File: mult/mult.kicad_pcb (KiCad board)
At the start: 2 copper layers, 20 x 108 mm, 72 parts, among them J1 Eurorack_Mono_Jack, J10 Eurorack_Mono_Jack, J11 Eurorack_Mono_Jack_No_S, J12 Eurorack_Mono_Jack_No_S, J13 Eurorack_Mono_Jack, J14 Eurorack_Mono_Jack, J15 Eurorack_Mono_Jack_No_S, J16 Eurorack_Mono_Jack_No_S, J17 Eurorack_Power, J2 Eurorack_Mono_Jack, J3 Eurorack_Mono_Jack_No_S, J4 Eurorack_Mono_Jack_No_S, J6 Eurorack_Mono_Jack, J7 Eurorack_Mono_Jack_No_S, J8 Eurorack_Mono_Jack_No_S, J9 Eurorack_Mono_Jack, U1 OPA1679, U2 OPA1679, U3 OPA1679, U4 OPA1679

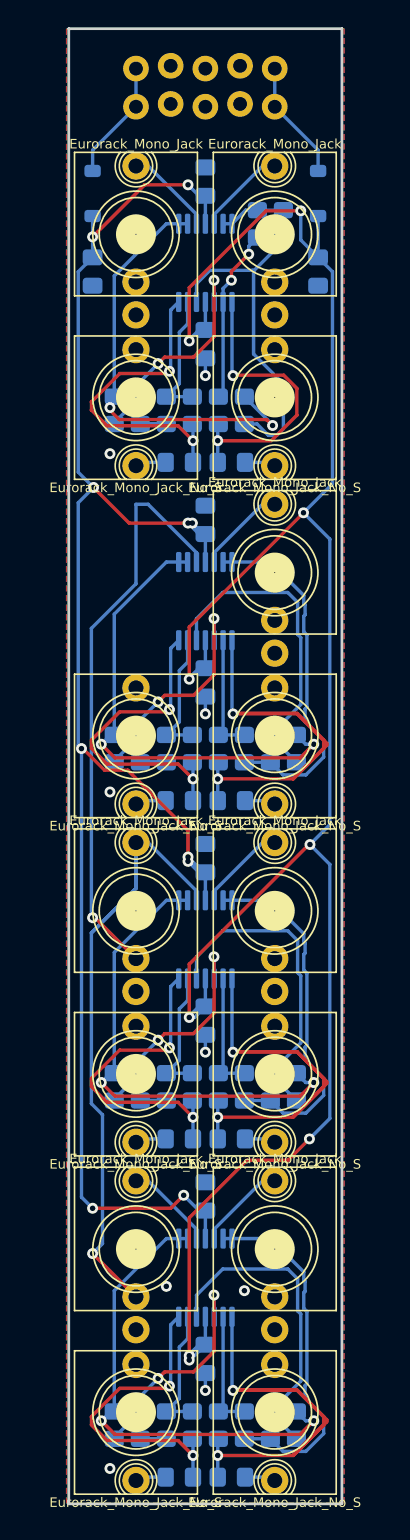
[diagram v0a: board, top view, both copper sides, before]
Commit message: mult: Place power diodes and caps closer to center
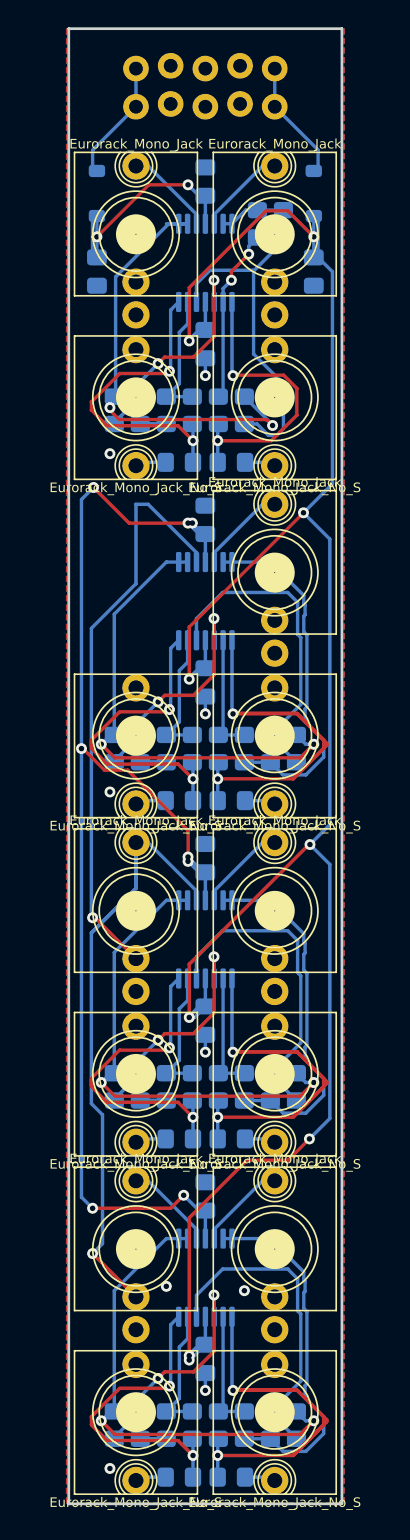
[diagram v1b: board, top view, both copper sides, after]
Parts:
- moved C9 0.32 mm to (2.22, 17.8)
- moved D1 0.32 mm to (2.22, 12.1)
- moved C10 0.32 mm to (18.1, 17.8)
- moved D2 0.32 mm to (18.1, 12.1)
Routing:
- net VCC: track 125.9 -> 114.0 mm
- net Net-(U1A--): track 32.3 -> 33.1 mm
- net VEE: track 158.8 -> 159.6 mm

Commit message: mult: Finish first layout pass, passes DRC errors
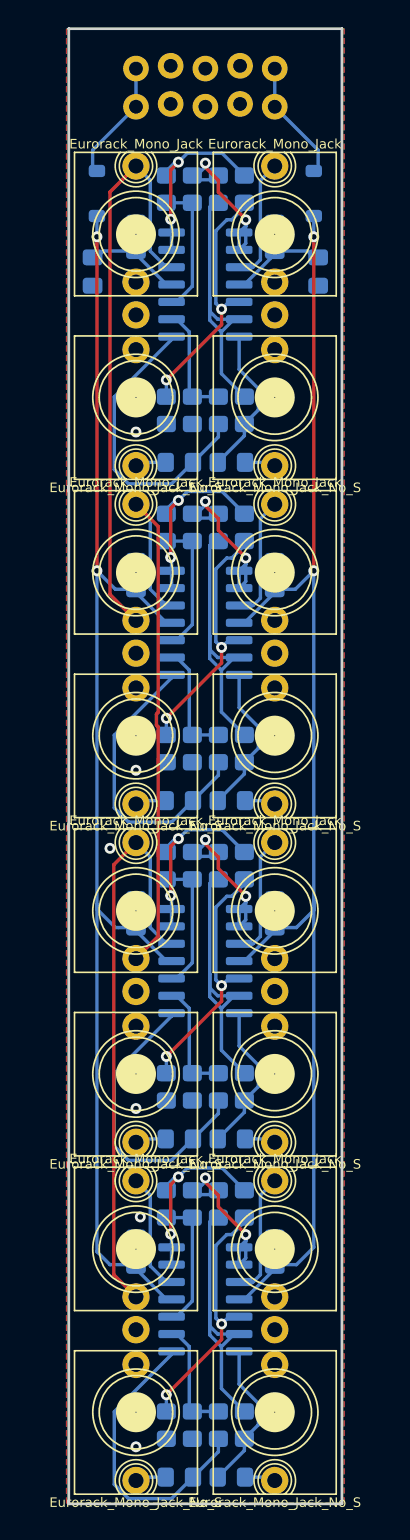
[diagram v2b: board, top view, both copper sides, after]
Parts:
- added J5: Eurorack_Mono_Jack, winterbloom:AudioJack_WQP518MA_Compact_S, F.Cu at (5.08, 39.8)
- U1, U2, U3, U4: footprint Package_SO:TSSOP-14_4.4x5mm_P0.65mm -> Package_SO:SOIC-14_3.9x8.7mm_P1.27mm
- moved R4 18.8 mm to (13.0, 11.7)
- moved R11 18.8 mm to (7.30, 36.5)
- moved R14 18.8 mm to (13.0, 36.5)
- moved R21 18.8 mm to (7.30, 61.3)
- moved R24 18.8 mm to (13.0, 61.3)
- moved R31 18.8 mm to (7.30, 86.0)
- moved R34 18.8 mm to (13.0, 86.0)
- moved R1 17.2 mm to (7.30, 11.7)
- moved R12 17.2 mm to (9.21, 36.5), turned to -90 degrees
- moved R22 17.2 mm to (9.21, 61.3), turned to -90 degrees
- moved R32 17.2 mm to (9.21, 86.0), turned to -90 degrees
- moved R13 16.3 mm to (11.1, 36.5), turned to 90 degrees
- moved R23 16.3 mm to (11.1, 61.3), turned to 90 degrees
- moved R33 16.3 mm to (11.1, 86.0), turned to 90 degrees
- moved C6 9.35 mm to (15.2, 64.8), turned to 90 degrees
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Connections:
- R1 pad 1: Net-(U1D-+) -> Net-(U1A-+)
- R1 pad 2: Net-(U1A--) -> Net-(U1B--)
- R10 pad 2: Net-(U1D--) -> Net-(U1A--)
- R11 pad 1: Net-(U2D-+) -> Net-(U2A-+)
- R11 pad 2: Net-(U2A--) -> Net-(U2B--)
- R12 pad 1: Net-(U2B--) -> Net-(U2C--)
- R12 pad 2: Net-(U2D-+) -> Net-(U2A-+)
- R13 pad 1: Net-(U2C--) -> Net-(U2D--)
- R13 pad 2: Net-(U2B--) -> Net-(U2C--)
- R14 pad 1: Net-(U2C-+) -> Net-(U2D-+)
- R14 pad 2: Net-(U2A--) -> Net-(U2B--)
- R17 pad 1: Net-(U2D--) -> Net-(U2A--)
- R18 pad 2: Net-(U2C-+) -> Net-(U2D-+)
- R19 pad 1: Net-(U2C--) -> Net-(U2D--)
- R2 pad 1: Net-(U1B--) -> Net-(U1C--)
- R2 pad 2: Net-(U1D-+) -> Net-(U1A-+)
- R20 pad 2: Net-(U2D--) -> Net-(U2A--)
- R21 pad 1: Net-(U3D-+) -> Net-(U3A-+)
- R21 pad 2: Net-(U3A--) -> Net-(U3B--)
- R22 pad 1: Net-(U3B--) -> Net-(U3C--)
- R22 pad 2: Net-(U3D-+) -> Net-(U3A-+)
- R23 pad 1: Net-(U3C--) -> Net-(U3D--)
- R23 pad 2: Net-(U3B--) -> Net-(U3C--)
- R24 pad 1: Net-(U3C-+) -> Net-(U3D-+)
- R24 pad 2: Net-(U3A--) -> Net-(U3B--)
- R27 pad 1: Net-(U3D--) -> Net-(U3A--)
- R28 pad 2: Net-(U3C-+) -> Net-(U3D-+)
- R29 pad 1: Net-(U3C--) -> Net-(U3D--)
- R3 pad 1: Net-(U1C--) -> Net-(U1D--)
- R3 pad 2: Net-(U1B--) -> Net-(U1C--)
- R30 pad 2: Net-(U3D--) -> Net-(U3A--)
- R31 pad 1: Net-(U4D-+) -> Net-(U4A-+)
- R31 pad 2: Net-(U4A--) -> Net-(U4B--)
- R32 pad 1: Net-(U4B--) -> Net-(U4C--)
- R32 pad 2: Net-(U4D-+) -> Net-(U4A-+)
- R33 pad 1: Net-(U4C--) -> Net-(U4D--)
- R33 pad 2: Net-(U4B--) -> Net-(U4C--)
- R34 pad 1: Net-(U4C-+) -> Net-(U4D-+)
- R34 pad 2: Net-(U4A--) -> Net-(U4B--)
- R37 pad 1: Net-(U4D--) -> Net-(U4A--)
- R38 pad 2: Net-(U4C-+) -> Net-(U4D-+)
- R39 pad 1: Net-(U4C--) -> Net-(U4D--)
- R4 pad 1: Net-(U1C-+) -> Net-(U1D-+)
- R4 pad 2: Net-(U1A--) -> Net-(U1B--)
- R40 pad 2: Net-(U4D--) -> Net-(U4A--)
- R7 pad 1: Net-(U1D--) -> Net-(U1A--)
- R8 pad 2: Net-(U1C-+) -> Net-(U1D-+)
- R9 pad 1: Net-(U1C--) -> Net-(U1D--)
- U1 pad 1: Net-(U1A--) -> Net-(R5-Pad1)
- U1 pad 10: Net-(U1C-+) -> Net-(J2-Tip)
- U1 pad 14: Net-(R5-Pad1) -> Net-(R6-Pad1)
- U1 pad 3: /channel 1/tip in (a) -> Net-(U1A-+)
- U1 pad 5: Net-(J2-Tip) -> /channel 1/tip in (a)
- U1 pad 8: Net-(R6-Pad1) -> Net-(U1C--)
- U2 pad 1: Net-(U2A--) -> Net-(R15-Pad1)
- U2 pad 10: Net-(U2C-+) -> Net-(J6-Tip)
- U2 pad 14: Net-(R15-Pad1) -> Net-(R16-Pad1)
- U2 pad 3: /channel 2/tip in (a) -> Net-(U2A-+)
- U2 pad 5: Net-(J6-Tip) -> /channel 2/tip in (a)
- U2 pad 8: Net-(R16-Pad1) -> Net-(U2C--)
- U3 pad 1: Net-(U3A--) -> Net-(R25-Pad1)
- U3 pad 10: Net-(U3C-+) -> Net-(J10-Tip)
- U3 pad 14: Net-(R25-Pad1) -> Net-(R26-Pad1)
- U3 pad 3: /channel 3/tip in (a) -> Net-(U3A-+)
- U3 pad 5: Net-(J10-Tip) -> /channel 3/tip in (a)
- U3 pad 8: Net-(R26-Pad1) -> Net-(U3C--)
- U4 pad 1: Net-(U4A--) -> Net-(R35-Pad1)
- U4 pad 10: Net-(U4C-+) -> Net-(J14-Tip)
- U4 pad 14: Net-(R35-Pad1) -> Net-(R36-Pad1)
- U4 pad 3: /channel 4/tip in (a) -> Net-(U4A-+)
- U4 pad 5: Net-(J14-Tip) -> /channel 4/tip in (a)
- U4 pad 8: Net-(R36-Pad1) -> Net-(U4C--)
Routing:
- net VEE: track 159.6 -> 103.4 mm, vias 9 -> 2
- net /channel 1/tip in (a): track 6.58 -> 43.2 mm
- net Net-(U4A--): track 34.7 -> 7.73 mm, vias 2 -> 0
- net Net-(U3A--): track 34.7 -> 7.73 mm, vias 2 -> 0
- net Net-(U2A--): track 34.7 -> 7.73 mm, vias 2 -> 0
- net Net-(U1A--): track 33.1 -> 7.73 mm, vias 2 -> 0
- net Net-(R16-Pad1): track 36.4 -> 11.0 mm, vias 2 -> 0
- net Net-(R26-Pad1): track 36.4 -> 11.0 mm, vias 2 -> 0
- net Net-(R36-Pad1): track 36.4 -> 11.0 mm, vias 2 -> 0
- net GND: track 20.5 -> 0.00 mm, vias 9 -> 6
- net Net-(U4C-+): track 16.3 -> 0.00 mm, vias 2 -> 0
- net Net-(U3C-+): track 16.3 -> 0.00 mm, vias 2 -> 0
- net Net-(U1C-+): track 16.3 -> 0.00 mm, vias 2 -> 0
- net Net-(U2C-+): track 16.3 -> 0.00 mm, vias 2 -> 0
- net Net-(U3B--): track 26.3 -> 13.3 mm, vias 0 -> 2
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
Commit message: mult: Move diodes and caps away from jack pads
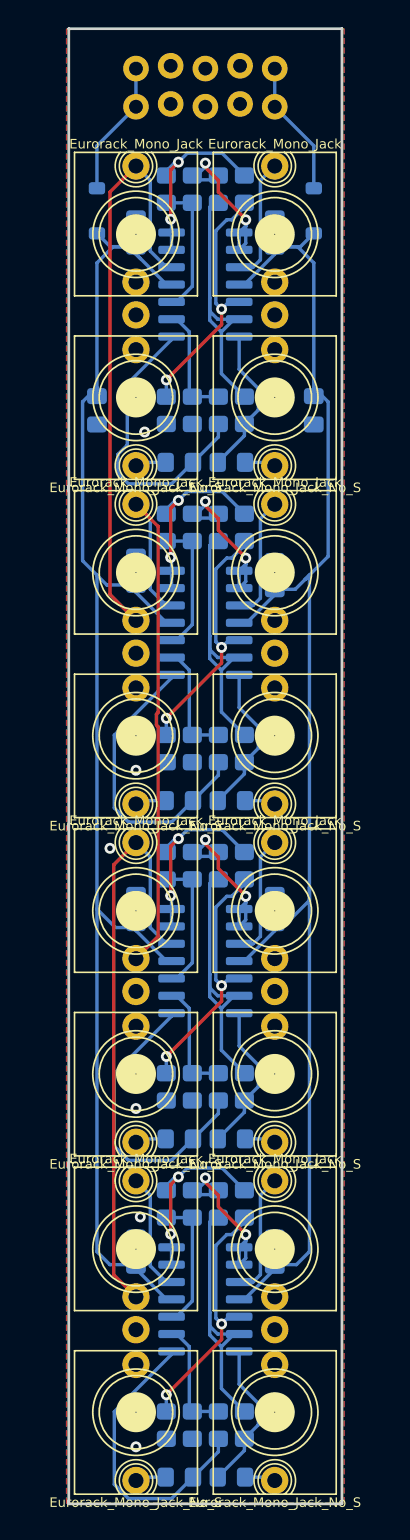
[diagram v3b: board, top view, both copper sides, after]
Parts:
- moved C10 10.2 mm to (18.1, 27.9)
- moved C9 10.2 mm to (2.22, 27.9)
- moved D1 1.27 mm to (2.22, 13.3)
- moved D2 1.27 mm to (18.1, 13.3)
- moved C3 0.32 mm to (5.08, 39.7)
- moved C1 0.32 mm to (5.08, 14.9)
- moved C2 0.32 mm to (15.2, 14.9)
- moved C5 0.32 mm to (5.08, 64.5)
- moved C6 0.32 mm to (15.2, 64.5)
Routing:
- net Net-(D2-K): track 8.81 -> 9.95 mm
- net Net-(D1-A): track 8.81 -> 9.95 mm
- net VCC: track 103.3 -> 104.3 mm, vias 2 -> 0
- net VEE: track 103.4 -> 103.9 mm, vias 2 -> 0

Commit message: mult: Move power diodes closer to header
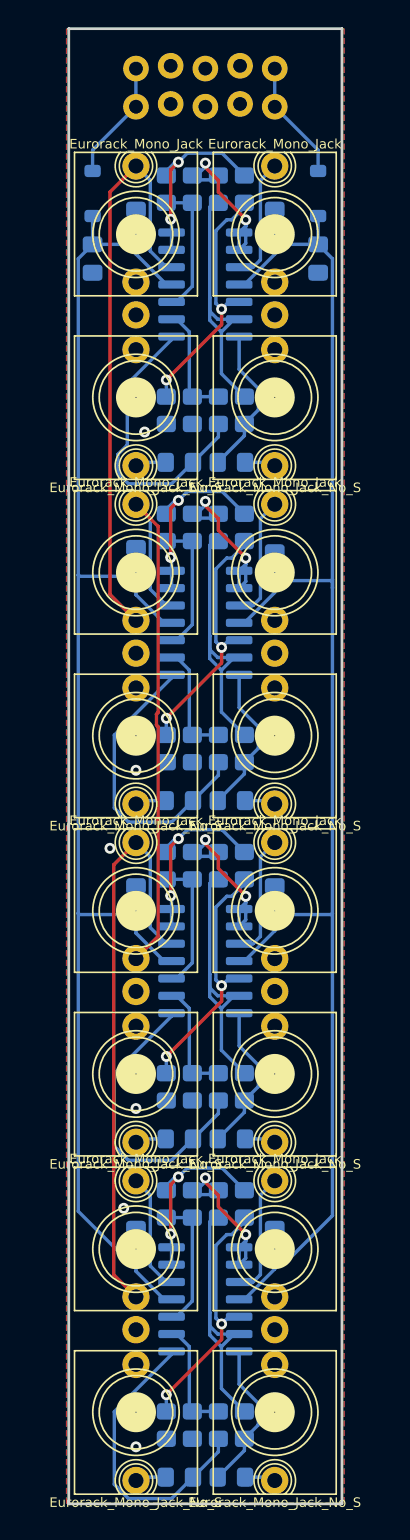
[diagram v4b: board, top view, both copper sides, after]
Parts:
- moved C10 11.1 mm to (18.4, 16.8)
- moved C9 11.1 mm to (1.91, 16.8)
- moved D1 1.31 mm to (1.91, 12.1)
- moved D2 1.31 mm to (18.4, 12.1)
- moved C4 0.64 mm to (15.2, 39.4)
- moved C1 0.63 mm to (5.08, 14.3)
- moved C2 0.63 mm to (15.2, 14.3)
- moved C3 0.63 mm to (5.08, 39.1)
- moved C5 0.63 mm to (5.08, 63.8)
- moved C6 0.63 mm to (15.2, 63.8)
- moved C7 0.63 mm to (5.08, 88.9)
- moved C8 0.63 mm to (15.2, 88.9)
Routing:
- net VEE: track 103.9 -> 108.2 mm
- net VCC: track 104.3 -> 107.0 mm
- net Net-(D2-K): track 9.95 -> 8.81 mm
- net Net-(D1-A): track 9.95 -> 8.81 mm
